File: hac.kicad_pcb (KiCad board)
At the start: 2 copper layers, 11 parts, among them J1 AudioJack3_Ground, U1 STM32F405RGTx, U2 TLV320AIC23BPW

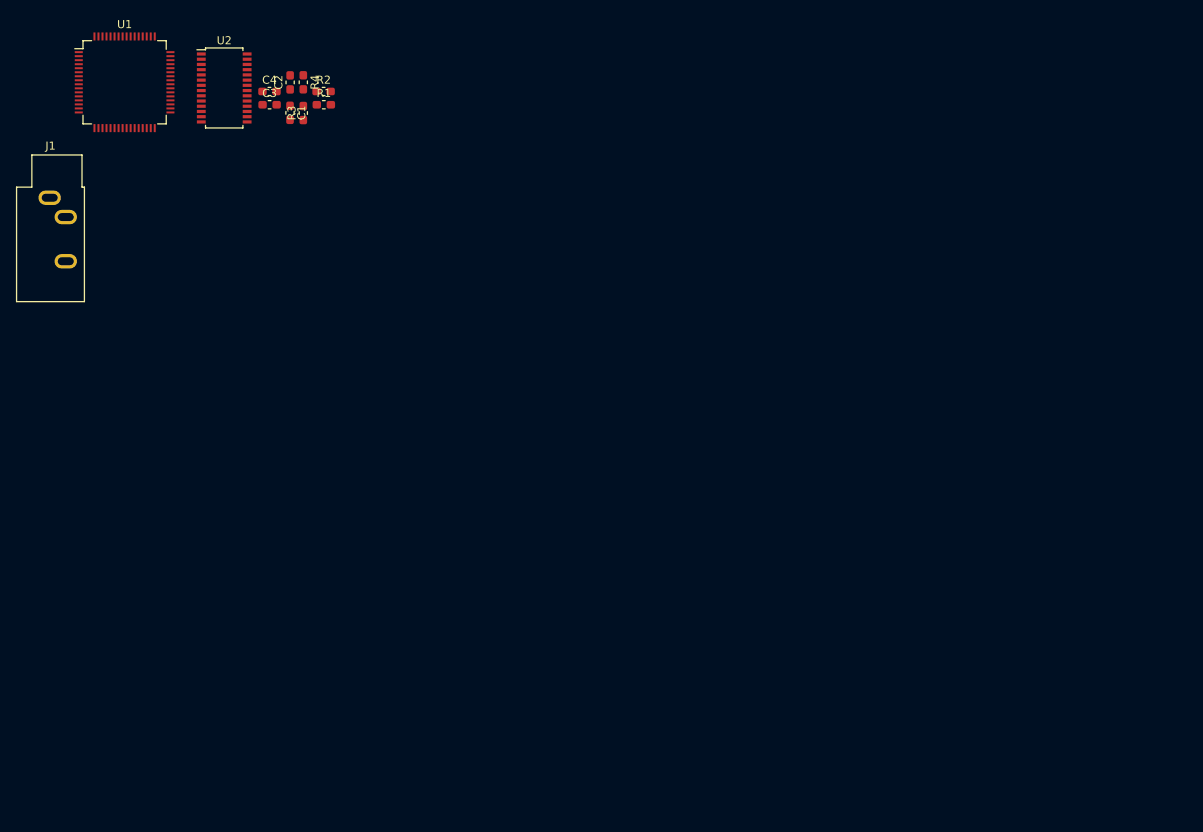
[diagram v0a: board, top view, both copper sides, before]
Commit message: schm fixes + footprints done
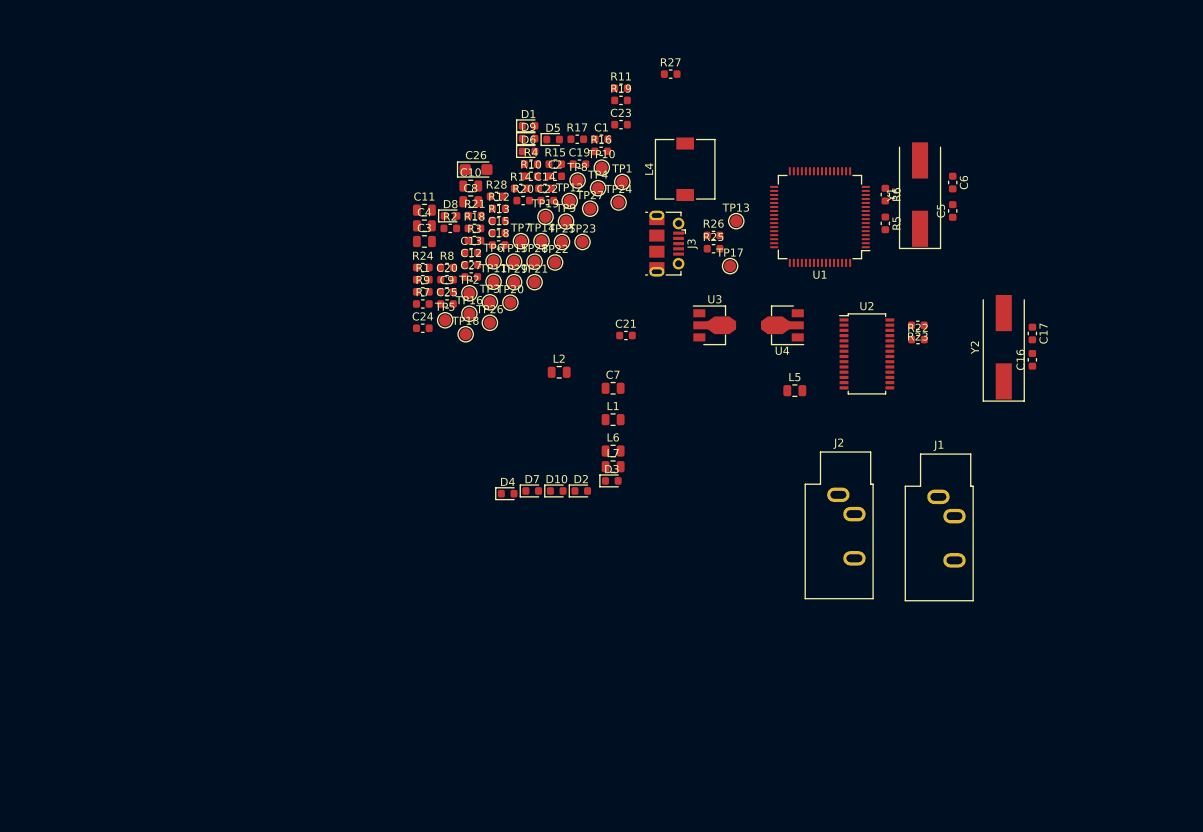
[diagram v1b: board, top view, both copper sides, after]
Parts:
- added C10: 1u, Capacitor_SMD:C_0805_2012Metric, F.Cu at (115.3, 74.1)
- added C11: 1u, Capacitor_SMD:C_0805_2012Metric, F.Cu at (109.6, 77.1)
- added C12: 100n, Capacitor_SMD:C_0603_1608Metric, F.Cu at (115.4, 83.9)
- added C13: 100n, Capacitor_SMD:C_0603_1608Metric, F.Cu at (115.4, 82.4)
- added C14: 100n, Capacitor_SMD:C_0603_1608Metric, F.Cu at (124.5, 74.4)
- added C15: 100n, Capacitor_SMD:C_0603_1608Metric, F.Cu at (118.8, 79.9)
- added C16: 20p, Capacitor_SMD:C_0603_1608Metric, F.Cu at (185.2, 95.7)
- added C17: 20p, Capacitor_SMD:C_0603_1608Metric, F.Cu at (185.2, 92.5)
- added C18: 100n, Capacitor_SMD:C_0603_1608Metric, F.Cu at (118.8, 81.4)
- added C19: 100n, Capacitor_SMD:C_0603_1608Metric, F.Cu at (128.8, 71.4)
- added C20: 330n, Capacitor_SMD:C_0603_1608Metric, F.Cu at (112.4, 85.8)
- added C21: 330n, Capacitor_SMD:C_0603_1608Metric, F.Cu at (134.6, 92.7)
- added C22: 100n, Capacitor_SMD:C_0603_1608Metric, F.Cu at (124.8, 75.9)
- added C23: 100n, Capacitor_SMD:C_0603_1608Metric, F.Cu at (134.0, 66.5)
- added C24: 100n, Capacitor_SMD:C_0603_1608Metric, F.Cu at (109.4, 91.8)
- added C25: 100n, Capacitor_SMD:C_0603_1608Metric, F.Cu at (112.4, 88.8)
- added C26: 10u, Capacitor_Tantalum_SMD:CP_EIA-3216-18_Kemet-A, F.Cu at (116.0, 72.1)
- added C27: 100n, Capacitor_SMD:C_0603_1608Metric, F.Cu at (115.4, 85.4)
- added C5: 20p, Capacitor_SMD:C_0603_1608Metric, F.Cu at (175.3, 77.2)
- added C6: 20p, Capacitor_SMD:C_0603_1608Metric, F.Cu at (175.3, 73.7)
- added C7: 2.2u, Capacitor_SMD:C_0805_2012Metric, F.Cu at (133.0, 99.3)
- added C8: 2.2u, Capacitor_SMD:C_0805_2012Metric, F.Cu at (115.3, 76.1)
- added C9: 100n, Capacitor_SMD:C_0603_1608Metric, F.Cu at (112.4, 87.3)
- added D1: 0, LED_SMD:LED_0603_1608Metric, F.Cu at (122.5, 66.6)
- added D10: 3.3VA, LED_SMD:LED_0603_1608Metric, F.Cu at (126.0, 112.0)
- added D2: 1, LED_SMD:LED_0603_1608Metric, F.Cu at (129.1, 112.0)
- added D3: 2, LED_SMD:LED_0603_1608Metric, F.Cu at (132.9, 110.8)
- added D4: 3, LED_SMD:LED_0603_1608Metric, F.Cu at (119.9, 112.4)
- added D5: 4, LED_SMD:LED_0603_1608Metric, F.Cu at (125.6, 68.3)
- added D6: 5, LED_SMD:LED_0603_1608Metric, F.Cu at (122.5, 69.8)
- added D7: 6, LED_SMD:LED_0603_1608Metric, F.Cu at (123.0, 112.0)
- added D8: 7, LED_SMD:LED_0603_1608Metric, F.Cu at (112.8, 77.8)
- added D9: 3.3V, LED_SMD:LED_0603_1608Metric, F.Cu at (122.5, 68.2)
- added J2: Line OUT, Connector_Audio:Jack_3.5mm_CUI_SJ1-3533NG_Horizontal, F.Cu at (161.0, 112.5)
- added J3: USB_B_Micro, Connector_USB:USB_Micro-B_Molex-105017-0001, F.Cu at (139.7, 81.3)
- added L1: FB, Inductor_SMD:L_0805_2012Metric, F.Cu at (133.0, 103.2)
- added L2: FB, Inductor_SMD:L_0805_2012Metric, F.Cu at (126.3, 97.3)
- added L4: 1m, Inductor_SMD:L_7.3x7.3_H4.5, F.Cu at (142.0, 72.0)
- added L5: FB, Inductor_SMD:L_0805_2012Metric, F.Cu at (155.6, 99.6)
- added L6: FB, Inductor_SMD:L_0805_2012Metric, F.Cu at (133.0, 107.1)
- added L7: FB, Inductor_SMD:L_0805_2012Metric, F.Cu at (133.0, 109.0)
- added R10: 1k, Resistor_SMD:R_0603_1608Metric, F.Cu at (122.8, 72.9)
- added R11: 1k, Resistor_SMD:R_0603_1608Metric, F.Cu at (134.0, 62.0)
- added R12: 1k, Resistor_SMD:R_0603_1608Metric, F.Cu at (118.8, 76.9)
- added R13: 1k, Resistor_SMD:R_0603_1608Metric, F.Cu at (118.8, 78.4)
- added R14: 1k, Resistor_SMD:R_0603_1608Metric, F.Cu at (121.5, 74.4)
- added R15: 1k, Resistor_SMD:R_0603_1608Metric, F.Cu at (125.8, 71.4)
- added R16: 100k, Resistor_SMD:R_0603_1608Metric, F.Cu at (131.5, 69.8)
- added R17: 100k, Resistor_SMD:R_0603_1608Metric, F.Cu at (128.6, 68.3)
- added R18: 0, Resistor_SMD:R_0603_1608Metric, F.Cu at (115.8, 79.4)
- added R19: 0, Resistor_SMD:R_0603_1608Metric, F.Cu at (134.0, 63.5)
- added R20: DNP, Resistor_SMD:R_0603_1608Metric, F.Cu at (121.8, 75.9)
- added R21: DNP, Resistor_SMD:R_0603_1608Metric, F.Cu at (115.8, 77.8)
- added R22: 0, Resistor_SMD:R_0603_1608Metric, F.Cu at (170.9, 93.2)
- added R23: 0, Resistor_SMD:R_0603_1608Metric, F.Cu at (170.9, 91.4)
- added R24: 100k, Resistor_SMD:R_0603_1608Metric, F.Cu at (109.4, 84.3)
- added R25: 0, Resistor_SMD:R_0603_1608Metric, F.Cu at (145.5, 81.9)
- added R26: 0, Resistor_SMD:R_0603_1608Metric, F.Cu at (145.5, 80.3)
- added R27: 1k, Resistor_SMD:R_0603_1608Metric, F.Cu at (140.2, 60.2)
- added R28: 1k, Resistor_SMD:R_0603_1608Metric, F.Cu at (118.5, 75.4)
- added R5: 0, Resistor_SMD:R_0603_1608Metric, F.Cu at (166.9, 78.8)
- added R6: 220, Resistor_SMD:R_0603_1608Metric, F.Cu at (166.9, 75.2)
- added R7: 10k, Resistor_SMD:R_0603_1608Metric, F.Cu at (109.4, 88.8)
- added R8: 1k, Resistor_SMD:R_0603_1608Metric, F.Cu at (112.4, 84.3)
- added R9: 1k, Resistor_SMD:R_0603_1608Metric, F.Cu at (109.4, 87.3)
- added TP1: C3, TestPoint:TestPoint_Pad_D1.5mm, F.Cu at (134.2, 73.6)
- added TP10: I2S2WS, TestPoint:TestPoint_Pad_D1.5mm, F.Cu at (131.6, 71.8)
- added TP11: I2C2SD, TestPoint:TestPoint_Pad_D1.5mm, F.Cu at (118.2, 86.0)
- added TP12: SPICS, TestPoint:TestPoint_Pad_D1.5mm, F.Cu at (127.6, 76.0)
- added TP13: USBDM, TestPoint:TestPoint_Pad_D1.5mm, F.Cu at (148.3, 78.5)
- added TP14: I2S2CK, TestPoint:TestPoint_Pad_D1.5mm, F.Cu at (124.1, 81.0)
- added TP15: SPISCK, TestPoint:TestPoint_Pad_D1.5mm, F.Cu at (120.7, 83.5)
- added TP16: I2C2SDEXT, TestPoint:TestPoint_Pad_D1.5mm, F.Cu at (115.1, 90.0)
- added TP17: USBDP, TestPoint:TestPoint_Pad_D1.5mm, F.Cu at (147.6, 84.1)
- added TP18: SPIMISO, TestPoint:TestPoint_Pad_D1.5mm, F.Cu at (114.7, 92.6)
- added TP19: SPIMOSI, TestPoint:TestPoint_Pad_D1.5mm, F.Cu at (124.6, 78.0)
- added TP2: C2, TestPoint:TestPoint_Pad_D1.5mm, F.Cu at (115.1, 87.5)
- added TP20: I2S3SD, TestPoint:TestPoint_Pad_D1.5mm, F.Cu at (120.2, 88.6)
- added TP21: VUSB, TestPoint:TestPoint_Pad_D1.5mm, F.Cu at (123.3, 86.1)
- added TP22: LOUT, TestPoint:TestPoint_Pad_D1.5mm, F.Cu at (125.8, 83.6)
- added TP23: LIN, TestPoint:TestPoint_Pad_D1.5mm, F.Cu at (129.2, 81.1)
- added TP24: ROUT, TestPoint:TestPoint_Pad_D1.5mm, F.Cu at (133.7, 76.2)
- added TP25: RIN, TestPoint:TestPoint_Pad_D1.5mm, F.Cu at (126.7, 81.1)
- added TP26: 3.3V, TestPoint:TestPoint_Pad_D1.5mm, F.Cu at (117.7, 91.1)
- added TP27: 3.3VA, TestPoint:TestPoint_Pad_D1.5mm, F.Cu at (130.2, 76.9)
- added TP28: GNDD, TestPoint:TestPoint_Pad_D1.5mm, F.Cu at (123.3, 83.5)
- added TP29: GNDA, TestPoint:TestPoint_Pad_D1.5mm, F.Cu at (120.7, 86.1)
- added TP3: C1, TestPoint:TestPoint_Pad_D1.5mm, F.Cu at (117.7, 88.6)
- added TP4: I2SMCK, TestPoint:TestPoint_Pad_D1.5mm, F.Cu at (131.2, 74.4)
- added TP5: BOOT0, TestPoint:TestPoint_Pad_D1.5mm, F.Cu at (112.1, 90.8)
- added TP6: C0, TestPoint:TestPoint_Pad_D1.5mm, F.Cu at (118.2, 83.5)
- added TP7: NRST, TestPoint:TestPoint_Pad_D1.5mm, F.Cu at (121.6, 81.0)
- added TP8: I2S3WS, TestPoint:TestPoint_Pad_D1.5mm, F.Cu at (128.6, 73.4)
- added TP9: I2S3CK, TestPoint:TestPoint_Pad_D1.5mm, F.Cu at (127.2, 78.5)
- added U3: L78L33_SOT89, Package_TO_SOT_SMD:SOT-89-3, F.Cu at (145.2, 91.4)
- added U4: L78L33_SOT89, Package_TO_SOT_SMD:SOT-89-3, F.Cu at (154.5, 91.4)
- added Y1: 8MHz, Crystal:Crystal_SMD_HC49-SD, F.Cu at (171.2, 75.2)
- added Y2: 12MHz, Crystal:Crystal_SMD_HC49-SD, F.Cu at (181.6, 94.2)
- C1, C2: footprint Capacitor_SMD:C_0603_1608Metric_Pad1.05x0.95mm_HandSolder -> Capacitor_SMD:C_0603_1608Metric
- C3, C4: footprint Capacitor_SMD:C_0603_1608Metric_Pad1.05x0.95mm_HandSolder -> Capacitor_SMD:C_0805_2012Metric
- J1: value AudioJack3_Ground -> Line IN
- R1, R2, R3, R4: footprint Resistor_SMD:R_0603_1608Metric_Pad1.05x0.95mm_HandSolder -> Resistor_SMD:R_0603_1608Metric
- moved J1 116.6 mm to (173.5, 112.8)
- moved U1 88.1 mm to (158.8, 78.0), turned to 180 degrees
- moved U2 86.5 mm to (164.6, 95.0)
- moved C1 38.9 mm to (131.6, 68.3), turned to 0 degrees
- moved C2 35.0 mm to (125.8, 72.9), turned to 0 degrees
- moved R4 30.1 mm to (122.8, 71.4), turned to 0 degrees
- moved R3 26.5 mm to (115.8, 80.9), turned to 0 degrees
- moved C3 25.7 mm to (109.6, 81.0)
- moved C4 25.5 mm to (109.6, 79.1)
- moved R1 25.0 mm to (109.4, 85.8)
- moved R2 23.2 mm to (112.8, 79.4)
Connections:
- U1 pad 1: Net-(U1-Pad1) -> Net-(C12-Pad1)
- U1 pad 12: Net-(U1-Pad12) -> GNDD
- U1 pad 13: Net-(U1-Pad13) -> Net-(C12-Pad1)
- U1 pad 18: Net-(U1-Pad18) -> GNDD
- U1 pad 19: Net-(U1-Pad19) -> Net-(C12-Pad1)
- U1 pad 20: Net-(U1-Pad20) -> SPI_CS
- U1 pad 21: Net-(U1-Pad21) -> SPI_SCK
- U1 pad 22: Net-(U1-Pad22) -> /SPI1_MISO
- U1 pad 23: Net-(U1-Pad23) -> SPI_MOSI
- U1 pad 32: Net-(U1-Pad32) -> Net-(C12-Pad1)
- U1 pad 33: Net-(U1-Pad33) -> I2S_WSI
- U1 pad 34: Net-(U1-Pad34) -> I2S_CK
- U1 pad 35: Net-(U1-Pad35) -> /I2S2ext_SD
- U1 pad 36: Net-(U1-Pad36) -> I2S_SDI
- U1 pad 37: Net-(U1-Pad37) -> I2S_MCK
- U1 pad 44: Net-(U1-Pad44) -> USB_DM
- U1 pad 45: Net-(U1-Pad45) -> USB_DP
- U1 pad 48: Net-(U1-Pad48) -> Net-(C12-Pad1)
- U1 pad 50: Net-(U1-Pad50) -> I2S_WSO
- U1 pad 55: Net-(U1-Pad55) -> /I2S3_CK
- U1 pad 57: Net-(U1-Pad57) -> /I2S3_SD
- U1 pad 63: Net-(U1-Pad63) -> GNDD
- U1 pad 64: Net-(U1-Pad64) -> Net-(C12-Pad1)
- U2 pad 1: Net-(U2-Pad1) -> Net-(C18-Pad1)
- U2 pad 11: Net-(U2-Pad11) -> GNDA
- U2 pad 12: Net-(U2-Pad12) -> LLINEOUT
- U2 pad 13: Net-(U2-Pad13) -> RLINEOUT
- U2 pad 21: Net-(U2-Pad21) -> SPI_CS
- U2 pad 22: Net-(U2-Pad22) -> +3V3
- U2 pad 23: Net-(U2-Pad23) -> SPI_MOSI
- U2 pad 24: Net-(U2-Pad24) -> SPI_SCK
- U2 pad 27: Net-(U2-Pad27) -> Net-(C18-Pad1)
- U2 pad 28: GND -> GNDD
- U2 pad 3: Net-(U2-Pad3) -> I2S_CK
- U2 pad 4: Net-(U2-Pad4) -> I2S_SDO
- U2 pad 5: Net-(U2-Pad5) -> I2S_WSO
- U2 pad 6: Net-(U2-Pad6) -> I2S_SDI
- U2 pad 7: Net-(U2-Pad7) -> I2S_WSI

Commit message: component placement done
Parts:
- added C28: 100u, Capacitor_Tantalum_SMD:CP_EIA-6032-28_Kemet-C, B.Cu at (136.1, 133.5)
- added C29: 100u, Capacitor_Tantalum_SMD:CP_EIA-6032-28_Kemet-C, B.Cu at (140.5, 133.5)
- added C30: 100n, Capacitor_SMD:C_0603_1608Metric, B.Cu at (159.7, 112.5)
- added H1: MountingHole, MountingHole:MountingHole_3.2mm_M3, F.Cu at (193.0, 74.3)
- added H2: MountingHole, MountingHole:MountingHole_3.2mm_M3, F.Cu at (124.0, 74.4)
- added H3: MountingHole, MountingHole:MountingHole_3.2mm_M3, F.Cu at (193.0, 146.1)
- added H4: MountingHole, MountingHole:MountingHole_3.2mm_M3, F.Cu at (124.0, 146.1)
- added J4: HPOUT, Connector_Audio:Jack_3.5mm_Neutrik_NMJ6HCD2_Horizontal, F.Cu at (129.9, 142.4)
- added R29: 100k, Resistor_SMD:R_0603_1608Metric, B.Cu at (133.1, 135.1)
- added R30: 100k, Resistor_SMD:R_0603_1608Metric, B.Cu at (141.2, 138.4)
- added R31: 3.3, Resistor_SMD:R_0603_1608Metric, B.Cu at (157.0, 115.1)
- added TP30: LHP, TestPoint:TestPoint_Pad_D1.5mm, F.Cu at (145.5, 120.4)
- added TP31: RHP, TestPoint:TestPoint_Pad_D1.5mm, F.Cu at (142.2, 119.9)
- C1, C10, C11, C12, C13, C14, C15, C18, C19, C2, C22, C23, C26, C27, C3, C4, C7, C8, C9, L1, L2, L5, R1, R16, R17, R2, R3, R4, R7: moved to B.Cu
- J1: value Line IN -> LIN; footprint Connector_Audio:Jack_3.5mm_CUI_SJ1-3533NG_Horizontal -> Connector_Audio:Jack_3.5mm_Neutrik_NMJ6HCD2_Horizontal
- J2: value Line OUT -> LOUT; footprint Connector_Audio:Jack_3.5mm_CUI_SJ1-3533NG_Horizontal -> Connector_Audio:Jack_3.5mm_Neutrik_NMJ6HCD2_Horizontal
- moved R4 88.7 mm to (179.1, 140.0), turned to 180 degrees
- moved R2 88.3 mm to (174.7, 142.2), turned to 180 degrees
- moved C4 87.2 mm to (178.1, 133.1), turned to 270 degrees
- moved C2 84.2 mm to (179.0, 138.2)
- moved R1 82.5 mm to (175.5, 135.1), turned to 270 degrees
- moved C3 80.2 mm to (175.3, 127.1), turned to 270 degrees
- moved C11 79.1 mm to (154.1, 142.5)
- moved R3 78.0 mm to (174.5, 132.3)
- moved R17 75.6 mm to (153.4, 139.7), turned to 270 degrees
- moved C1 75.4 mm to (174.5, 130.3), turned to 180 degrees
- moved C10 73.2 mm to (154.3, 136.1)
- moved R16 67.3 mm to (153.7, 133.3), turned to 270 degrees
- moved R21 63.5 mm to (168.9, 112.5), turned to 270 degrees
- moved C26 62.8 mm to (162.5, 114.3), turned to 180 degrees
- moved C23 58.1 mm to (163.3, 116.6), turned to 180 degrees
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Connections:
- net Net-(C12-Pad1) renamed /3V3_STM
- L5 pad 2: Net-(C22-Pad1) -> Net-(C30-Pad1)
- R10 pad 2: Net-(R10-Pad2) -> LED2
- R11 pad 2: Net-(R11-Pad2) -> LED3
- R12 pad 2: Net-(R12-Pad2) -> LED4
- R13 pad 2: Net-(R13-Pad2) -> LED5
- R14 pad 2: Net-(R14-Pad2) -> LED6
- R15 pad 2: Net-(R15-Pad2) -> LED7
- R8 pad 2: Net-(R8-Pad2) -> LED0
- R9 pad 2: Net-(R9-Pad2) -> LED1
- U1 pad 17: Net-(U1-Pad17) -> LED7
- U1 pad 2: Net-(R13-Pad2) -> Net-(U1-Pad2)
- U1 pad 24: Net-(U1-Pad24) -> LED6
- U1 pad 25: Net-(U1-Pad25) -> LED5
- U1 pad 26: Net-(U1-Pad26) -> LED4
- U1 pad 27: Net-(U1-Pad27) -> LED3
- U1 pad 28: Net-(U1-Pad28) -> LED2
- U1 pad 29: Net-(U1-Pad29) -> LED1
- U1 pad 3: Net-(R14-Pad2) -> Net-(U1-Pad3)
- U1 pad 30: Net-(U1-Pad30) -> LED0
- U1 pad 39: Net-(R8-Pad2) -> Net-(U1-Pad39)
- U1 pad 4: Net-(R15-Pad2) -> Net-(U1-Pad4)
- U1 pad 40: Net-(R9-Pad2) -> Net-(U1-Pad40)
- U1 pad 51: Net-(R10-Pad2) -> Net-(U1-Pad51)
- U1 pad 52: Net-(R11-Pad2) -> Net-(U1-Pad52)
- U1 pad 53: Net-(R12-Pad2) -> Net-(U1-Pad53)
- U2 pad 10: Net-(U2-Pad10) -> RHPOUT
- U2 pad 22: +3V3 -> Net-(C18-Pad1)
- U2 pad 8: Net-(U2-Pad8) -> Net-(C30-Pad1)
- U2 pad 9: Net-(U2-Pad9) -> LHPOUT
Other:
- board outline added: 77.7 x 80.3 mm

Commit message: some routing done
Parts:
- added TP32: CLKOUT, TestPoint:TestPoint_Pad_D1.5mm, F.Cu at (156.2, 105.7)
- C1, C10, C11, C2, C28, C29, C3, C4, R1, R16, R17, R2, R29, R3, R30, R4: moved to F.Cu
- moved C11 24.5 mm to (149.1, 118.5), turned to 90 degrees
- moved R2 23.7 mm to (185.6, 121.2), turned to 0 degrees
- moved R4 20.0 mm to (183.1, 120.4), turned to 270 degrees
- moved R17 19.2 mm to (148.4, 121.2), turned to 0 degrees
- moved R30 18.5 mm to (135.4, 120.9), turned to 0 degrees
- moved C29 18.1 mm to (136.1, 116.0)
- moved C28 18.0 mm to (140.2, 116.0)
- moved C2 17.9 mm to (181.4, 120.4), turned to 90 degrees
- moved C10 17.8 mm to (151.4, 118.5), turned to 90 degrees
- moved R29 16.2 mm to (141.0, 120.9), turned to 180 degrees
- moved C4 15.8 mm to (171.1, 118.9), turned to 0 degrees
- moved R1 14.2 mm to (178.3, 121.2), turned to 0 degrees
- moved R16 12.3 mm to (152.2, 121.2), turned to 180 degrees
- moved R3 12.0 mm to (175.8, 120.4), turned to 270 degrees
- moved TP22 11.8 mm to (150.1, 115.1)
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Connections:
- net USB_DM renamed USB_D-
- net USB_DP renamed USB_D+
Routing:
- net SPI_MOSI: track 0.00 -> 68.3 mm, vias 0 -> 2
- net SPI_CS: track 0.00 -> 64.6 mm
- net GND: track 0.00 -> 64.2 mm
- net SPI_SCK: track 0.00 -> 61.9 mm
- net I2S_MCK: track 0.00 -> 53.3 mm, vias 0 -> 6
- net I2S_CK: track 0.00 -> 52.9 mm, vias 0 -> 2
- net /SPI1_MISO: track 0.00 -> 50.1 mm
- net /3V3_STM: track 0.00 -> 45.4 mm, vias 0 -> 6
- net GNDD: track 0.00 -> 45.1 mm, vias 0 -> 11
- net I2S_WSI: track 0.00 -> 41.8 mm, vias 0 -> 2
- net USB_D+: track 0.00 -> 39.0 mm, vias 0 -> 2
- net I2S_SDI: track 0.00 -> 33.8 mm
- net USB_D-: track 0.00 -> 33.3 mm
- net GNDA: track 0.00 -> 32.5 mm, vias 0 -> 9
- net /I2S2ext_SD: track 0.00 -> 31.3 mm, vias 0 -> 2
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- added copper zone on F.Cu, net /3V3_STM
- added copper zone on B.Cu, net GNDA
- added copper zone on B.Cu, net GNDD

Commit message: routing almost done
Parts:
- added TP33: GND, TestPoint:TestPoint_Pad_D1.5mm, F.Cu at (122.6, 90.8)
- added TP34: GND, TestPoint:TestPoint_Pad_D1.5mm, F.Cu at (121.9, 102.1)
- added TP35: GNDD, TestPoint:TestPoint_Pad_D1.5mm, F.Cu at (169.5, 97.8)
- added TP36: GNDA, TestPoint:TestPoint_Pad_D1.5mm, F.Cu at (143.5, 118.1)
- added TP37: GNDD, TestPoint:TestPoint_Pad_D1.5mm, F.Cu at (175.3, 85.1)
- added TP38: GNDA, TestPoint:TestPoint_Pad_D1.5mm, F.Cu at (154.3, 118.1)
- added TP39: GNDD, TestPoint:TestPoint_Pad_D1.5mm, F.Cu at (144.5, 73.9)
- added TP40: GNDA, TestPoint:TestPoint_Pad_D1.5mm, F.Cu at (167.6, 123.2)
- added TP41: GNDD, TestPoint:TestPoint_Pad_D1.5mm, F.Cu at (150.4, 103.9)
- R7: moved to F.Cu
- moved R7 3.92 mm to (172.2, 95.1), turned to 270 degrees
- moved L5 0.77 mm to (156.2, 113.2)
- moved R31 0.65 mm to (157.1, 115.7)
- moved C21 0.38 mm to (139.9, 107.7)
- moved C30 0.26 mm to (159.5, 112.4)
- moved C22 0.13 mm to (159.8, 116.2)
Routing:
- net +3.3VA: track 8.50 -> 44.6 mm, vias 0 -> 1
- net +3V3: track 26.4 -> 51.5 mm, vias 1 -> 3
- net Net-(C20-Pad1): track 9.58 -> 21.3 mm, vias 0 -> 2
- net Net-(R7-Pad2): track 0.00 -> 11.0 mm
- net Net-(C18-Pad1): track 13.0 -> 20.6 mm, vias 3 -> 4
- net GNDA: track 32.5 -> 28.6 mm, vias 9 -> 155
- net Net-(C10-Pad1): track 18.4 -> 22.1 mm
- net I2S_CK: track 52.9 -> 55.3 mm
- net I2S_WSI: track 41.8 -> 39.8 mm
- net Net-(C28-Pad2): track 21.8 -> 23.7 mm
- net SPI_SCK: track 61.9 -> 63.2 mm
- net SPI_MOSI: track 68.3 -> 69.4 mm
- net GNDD: track 45.1 -> 46.3 mm, vias 11 -> 112
- net /I2S2ext_SD: track 31.3 -> 30.1 mm
- net I2S_SDI: track 33.8 -> 32.8 mm
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- added copper zone on F.Cu, net GND
- added copper zone on F.Cu, net GNDA
- added copper zone on F.Cu, net GNDD

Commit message: gerbers + fixes
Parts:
- moved TP37 0.28 mm to (175.4, 85.3)
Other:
- board text added: "1.0"
- board text added: "2CK"
- board text added: "2SD"
- board text added: "2SDext"
- board text added: "2WS"
- board text added: "3.3V"
- board text added: "3.3VA"
- board text added: "3CK"
- board text added: "3SD"
- board text added: "3WS"
- board text added: "BOOT0"
- board text added: "C0"
- board text added: "C1"
- board text added: "C2"
- board text added: "C3"
- board text added: "CLKOUT"
- board text added: "CS"
- board text added: "GND"
- board text added: "GNDA"
- board text added: "GNDD"
- board text added: "HAC"
- board text added: "LHP"
- board text added: "LIN"
- board text added: "LOUT"
- board text added: "MCK"
- board text added: "MISO"
- board text added: "MOSI"
- board text added: "NRST"
- board text added: "RHP"
- board text added: "RIN"
- board text added: "ROUT"
- board text added: "SCK"
- board text added: "USB D+"
- board text added: "USB D-"
- board text added: "VUSB"
- board text added: "https://github.com/JDRobotter/hac"
